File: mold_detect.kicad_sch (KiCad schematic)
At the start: 34 parts, among them J1 USB_C_Receptacle_USB2.0_14P, U1 SHT30-DIS, U2 TPL5010, U3 FT230XS, U4 W25Q128JVS, U5 ATmega328P-P

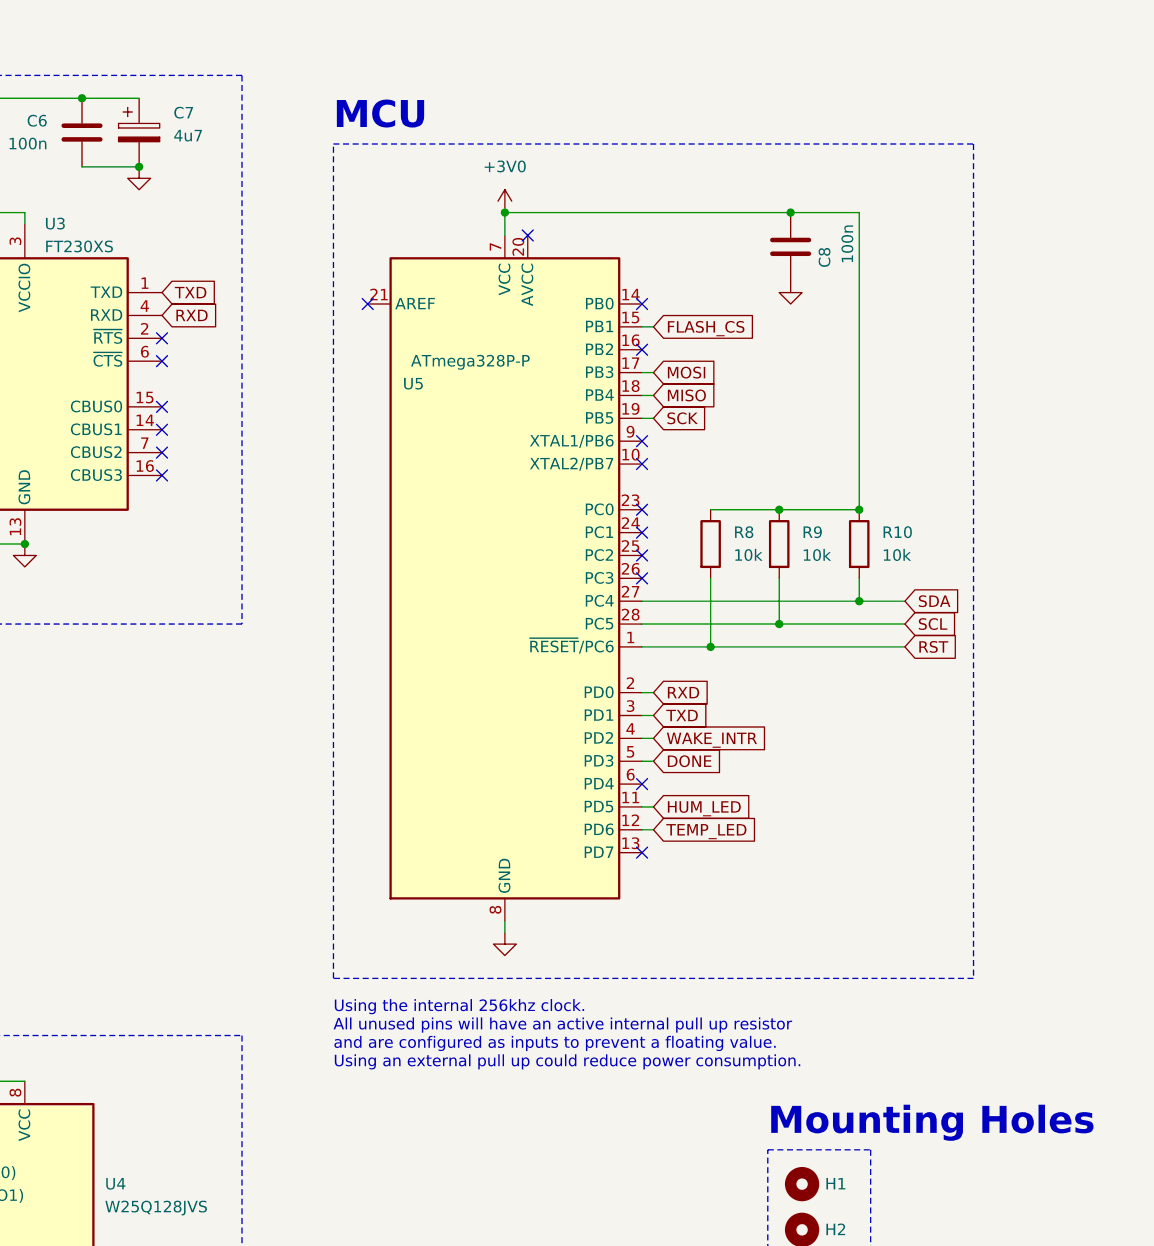
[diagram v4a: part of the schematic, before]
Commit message: added external oscillator
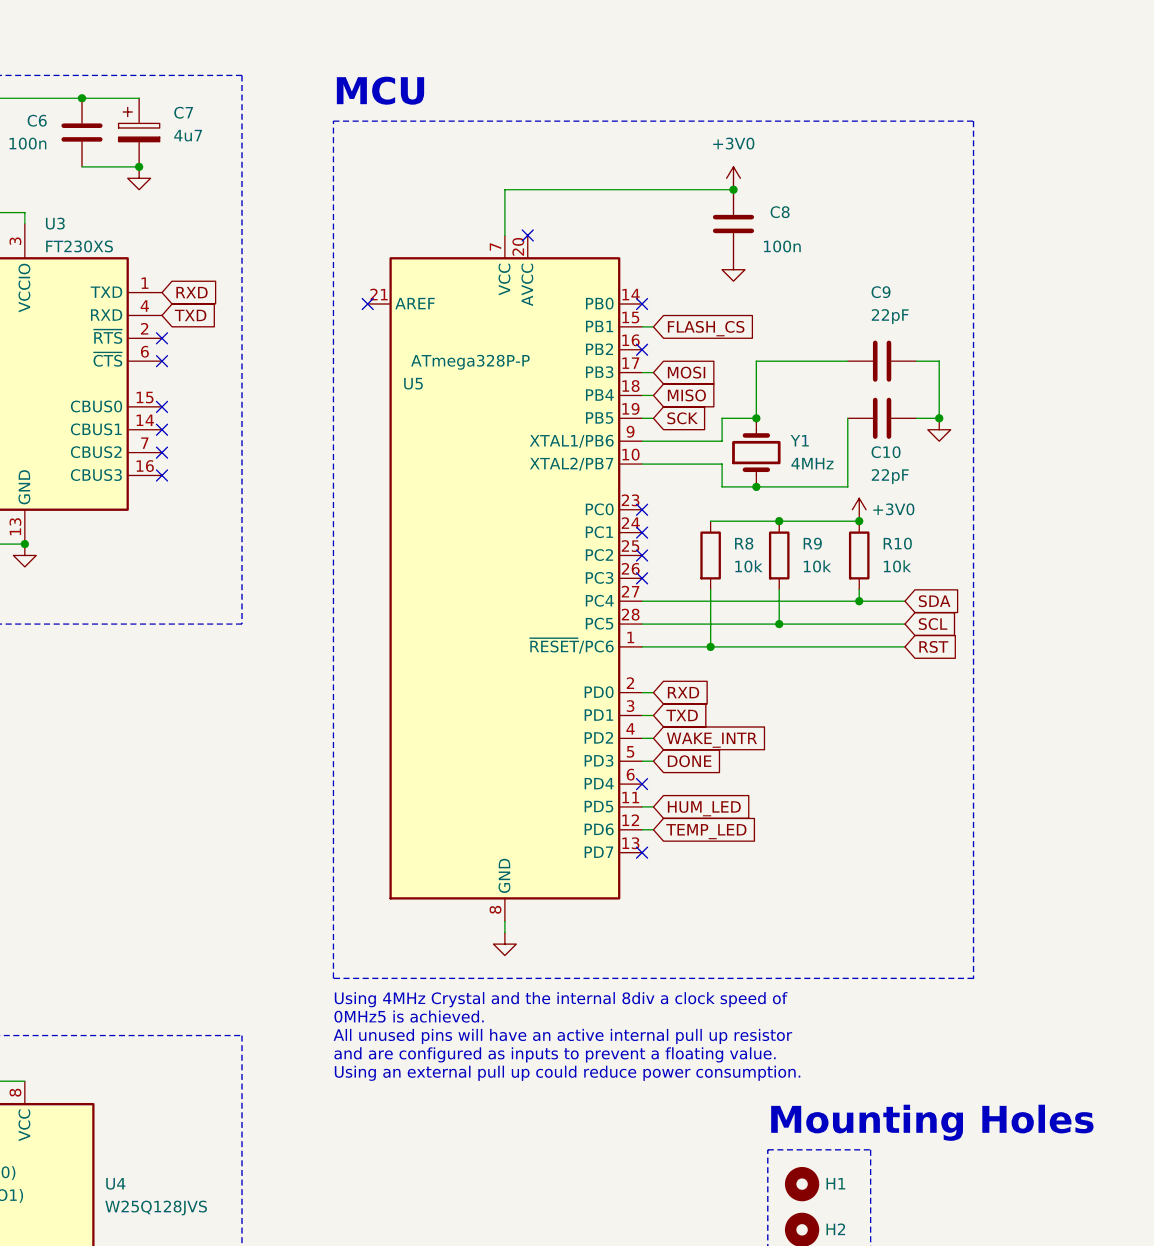
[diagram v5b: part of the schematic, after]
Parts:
- added C10, C9: 22pF, Capacitor_SMD:C_0603_1608Metric_Pad1.08x0.95mm_HandSolder, symbol Device:C
- added Y1: 4MHz, symbol Device:Crystal
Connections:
- net GND: now also C10.1, C9.1
- net RXD: now also U3.1 (TXD); no longer U3.4 (RXD)
- net TXD: now also U3.4 (RXD); no longer U3.1 (TXD)
- net at U5.10 (XTAL2/PB7): now also C10.2, Y1.1
- net at U5.9 (XTAL1/PB6): now also C9.2, Y1.2
- no-connect marks 20 -> 18
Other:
- note added: "Using 4MHz Crystal and the internal 8div a clock speed of 0MHz5 is achieved. All unused pins will have an active internal pull up resistor and are configured as inputs to prevent a floating value. Using an external pull up could reduce power consumption."
- note removed: "Using the internal 256khz clock. All unused pins will have an active internal pull up resistor and are configured as inputs to prevent a floating value. Using an external pull up could reduce power consumption."
- moved on the sheet: C8, R10, R8, R9

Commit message: the spi flash chip works
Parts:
- added C11: 100n, Capacitor_SMD:C_0603_1608Metric_Pad1.08x0.95mm_HandSolder, symbol Device:C
- added D2: D_Schottky, Diode_SMD:D_SOD-323_HandSoldering, symbol Device:D_Schottky
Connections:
- net +3V0: now also C11.2
- net FLASH_CS: now also U5.16 (PB2); no longer U5.15 (PB1)
- net GND: now also C11.1
- net at J1.A4 (VBUS), J1.A9 (VBUS), J1.B4 (VBUS)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: now also D2.2 (A); no longer C3.2, FB1.1
- net MISO renamed CIPO
- net MOSI renamed COPI
- new net: C3.2, D2.1 (K), FB1.1
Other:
- note added: "Battery"
- note added: "IO2 is write enable (turned off) IO3 is hold (turned off)"
- note added: "The *two* 5k1 resistors at the C1 and C2 pins configure the USB C port for USB 2.0 operation. These aren't used when using a USB-A to USB-C cable. The USB Bus Powered Configuration is used (data sheet p. 18). The diode is needed to prevent the initial 3V3 laying on the USB-C port's VBUS when using a USB-C to USB-C cable. Without this the USB-C host won't enable USB 2.0 at 5V operation."
- note added: "Using 4MHz crystal and the internal 8div a clock speed of 0MHz5 is achieved. The internal crystal isn't accurate enough for UART. All unused pins will have an active internal pull up resistor and are configured as inputs to prevent a floating value. Using an external pull up could reduce power consumption."
- note removed: "Power"
- note removed: "The *two* 5k1 resistors at the C1 and C2 pins configure the USB C port for USB 2.0 operation. The USB Bus Powered Configuration is used (data sheet p. 18)."
- note removed: "Using 4MHz Crystal and the internal 8div a clock speed of 0MHz5 is achieved. All unused pins will have an active internal pull up resistor and are configured as inputs to prevent a floating value. Using an external pull up could reduce power consumption."
